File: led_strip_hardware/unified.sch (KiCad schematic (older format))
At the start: 36 parts, among them P1 mod_jack_in, P2 PWR_TST, P3 LED_STRIP, P4 ICSP, Q1 FDN5618P, SW1 USR_SW, U1 ISL83485IBZ, U2 TPS54560, U3 STM32F030-32, U4 NCP1117ST33T3G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

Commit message: Progress on v7 of led_strip_hardware
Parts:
- added C10: 2u2, SM1210, symbol C-RESCUE-unified
- added C11: 2u2, SA0805, symbol C-RESCUE-unified
- added C12: 100n, SA0402, symbol C-RESCUE-unified
- C1: footprint (none) -> SM1210; symbol C -> C-RESCUE-unified
- C2, C3, C4, C5, C8: footprint (none) -> SA0402; symbol C -> C-RESCUE-unified
- C6, C7: footprint (none) -> B6; symbol C -> C-RESCUE-unified
- C9: footprint (none) -> SA0805; symbol C -> C-RESCUE-unified
- D1: footprint (none) -> SA0603_LED; symbol LED -> LED-RESCUE-unified
- D2: footprint (none) -> DPAK3
- D3: footprint (none) -> DO-214AA(SMB)
- L1: footprint (none) -> MSS1210
- P1: footprint (none) -> Assman-6p4c
- P2, P3, P4: footprint (none) -> SIL-4
- Q1: footprint (none) -> SOT23GDS
- R1, R11, R12: footprint (none) -> SA0603; symbol R -> R-RESCUE-unified
- R10, R2, R3, R4, R7, R8, R9: footprint (none) -> SA0402; symbol R -> R-RESCUE-unified
- R5: value 68K -> 270K; footprint (none) -> SA0402; symbol R -> R-RESCUE-unified
- R6: value 12K -> 22K; footprint (none) -> SA0402; symbol R -> R-RESCUE-unified
- SW1: footprint (none) -> TACT-SW-SMD
- U1: footprint (none) -> SO8E
- U2: footprint MODULE -> SO8_WITH_EP
- U3: footprint MODULE -> LQFP32
- U4: footprint (none) -> SOT223
- U5: footprint (none) -> SOT23
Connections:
- net +48V: now also C10.1
- net 3V3: now also C11.1, C12.1
- net GND: now also C10.2, C11.2, C12.2
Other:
- note added: "12K"
- note added: "12V"
- note added: "5V"
- note added: "68K"
- note added: "Iin=700mA\nVin=48V"
- note added: "Iout=5A\nVout=5V"
- note added: "Pd=1.2W"
- note added: "Pd=100mW"
- note added: "Pd=2W"
- note added: "Pd=50mW"
- note added: "Pd=750mW"
- note added: "R5"
- note added: "R6"
- note added: "Total Pd=4.2W"
- note added: "Vpp"

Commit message: Progress on v7 of led_strip_hardware; some lux utilities
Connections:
- net at U3.27 (PB4): now also SW1.3
- net at U3.30 (PB7): no longer SW1.3
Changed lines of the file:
@@
 	5550 1950 5550 2500
 Wire Wire Line
-	5400 2500 5550 2500
-Wire Wire Line
-	5550 2500 5700 2500
+	5400 2500 5700 2500
 Wire Wire Line
 	5700 2500 5700 2800
@@
 	5700 3400 5700 3200
 Wire Wire Line
-	5400 3400 5550 3400
-Wire Wire Line
-	5550 3400 5700 3400
+	5400 3400 5700 3400
 Wire Wire Line
 	5550 3400 5550 3500
@@
 Connection ~ 6600 2250
 Wire Wire Line
-	6600 1750 6950 1750
-Wire Wire Line
-	6950 1750 7200 1750
-Wire Wire Line
-	7200 1750 7400 1750
-Wire Wire Line
-	7400 1750 7800 1750
+	6600 1750 7800 1750
 Connection ~ 6600 1750
 Connection ~ 6950 1750
@@
 $EndComp
 Wire Wire Line
-	8200 2300 8300 2300
-Wire Wire Line
-	8300 2300 8550 2300
-Wire Wire Line
-	8550 2300 8800 2300
+	8200 2300 8800 2300
 $Comp
 L GND-RESCUE-unified #PWR014
@@
 $EndComp
 Wire Wire Line
-	6500 3900 6700 3900
-Wire Wire Line
-	6700 3900 7450 3900
-Wire Wire Line
-	6300 3800 6900 3800
-Wire Wire Line
-	6900 3800 7450 3800
+	6500 3900 7450 3900
+Wire Wire Line
+	6300 3800 7450 3800
 $Comp
 L GND-RESCUE-unified #PWR023
@@
 	4900 4100 4800 4100
 Wire Wire Line
-	4800 4050 4800 4100
-Wire Wire Line
-	4800 4100 4800 4150
+	4800 4050 4800 4150
 Connection ~ 4800 4100
 Wire Wire Line
@@
 2x 16SVPF82M
 Wire Wire Line
-	6100 4100 6100 3900
-Wire Wire Line
-	6100 3900 5300 3900
+	5300 3900 6400 3900
 Wire Wire Line
 	5300 3900 5300 4600
@@
 Connection ~ 2300 2350
 Wire Wire Line
-	1150 1850 1850 1850
-Wire Wire Line
-	1850 1850 2300 1850
-Wire Wire Line
-	2300 1850 2500 1850
+	1150 1850 2500 1850
 $Comp
 L +48V #PWR040
@@
 	2300 2350 2700 2350
 Wire Wire Line
-	2900 1850 3150 1850
-Wire Wire Line
-	3150 1850 3350 1850
-Wire Wire Line
-	3350 1850 3650 1850
+	2900 1850 3650 1850
 $Comp
 L DIODESCH D3
@@
 	2750 3700 2750 3850
 Wire Wire Line
-	2750 3850 3000 3850
-Wire Wire Line
-	3000 3850 3200 3850
-Wire Wire Line
-	2750 4350 3000 4350
-Wire Wire Line
-	3000 4350 3200 4350
+	2750 3850 3200 3850
+Wire Wire Line
+	2750 4350 3200 4350
 Wire Wire Line
 	2750 4350 2750 4550
@@
 R5
 Text Notes 6200 1150 0    60   ~ 0
+12V
+Text Notes 6200 1250 0    60   ~ 0
 5V
-Text Notes 6200 1250 0    60   ~ 0
-12V
 Text Notes 7050 1250 0    60   ~ 0
 68K
@@
 Text Notes 7450 1900 0    60   ~ 0
 Total Pd=4.2W
+Wire Wire Line
+	6400 3900 6400 4100
 $EndSCHEMATC

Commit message: LED strip hardware rev 7; ready for prod?
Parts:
- SW1: value USR_SW -> TL3315NF160Q
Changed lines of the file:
@@
 	3400 4050 3200 4050
 Wire Wire Line
-	3200 3850 3200 4050
+	3200 4050 3200 3850
 Wire Wire Line
 	1500 1950 1500 4000
@@
 P 2950 5600
 F 0 "SW1" H 2950 5900 60  0000 C CNN
-F 1 "USR_SW" H 2950 5450 60  0000 C CNN
+F 1 "TL3315NF160Q" H 2950 5450 60  0000 C CNN
 F 2 "TACT-SW-SMD" H 2950 5350 30  0000 C CNN
 F 3 "" H 2950 5600 60  0000 C CNN

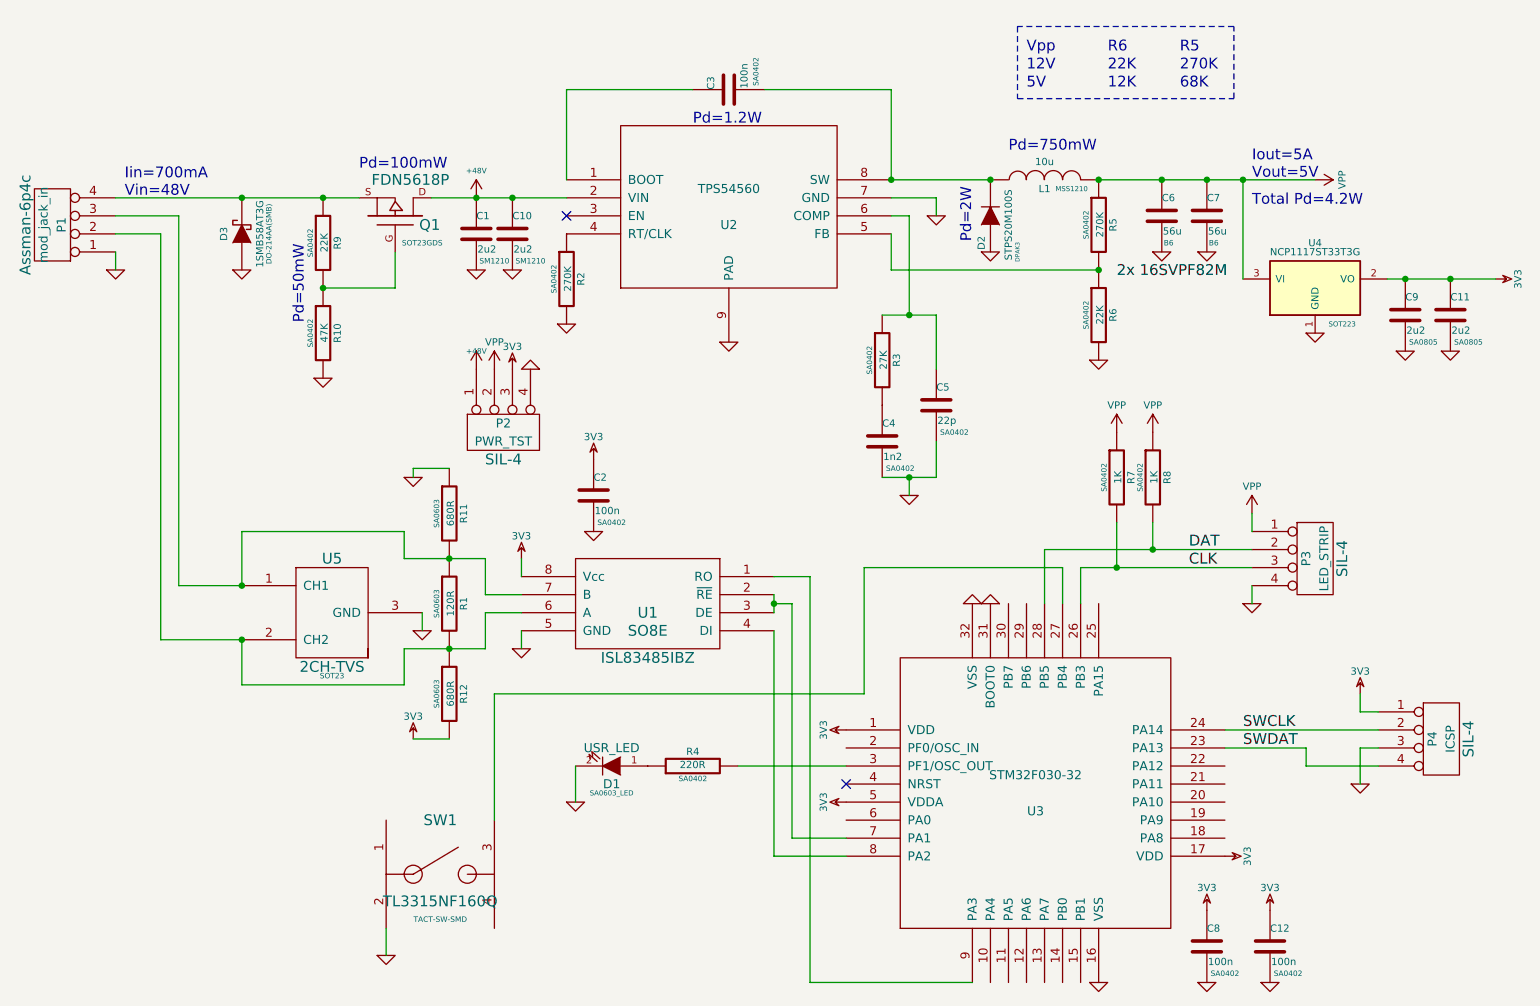
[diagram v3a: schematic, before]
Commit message: Flipped D2; still need to fix silk bottom
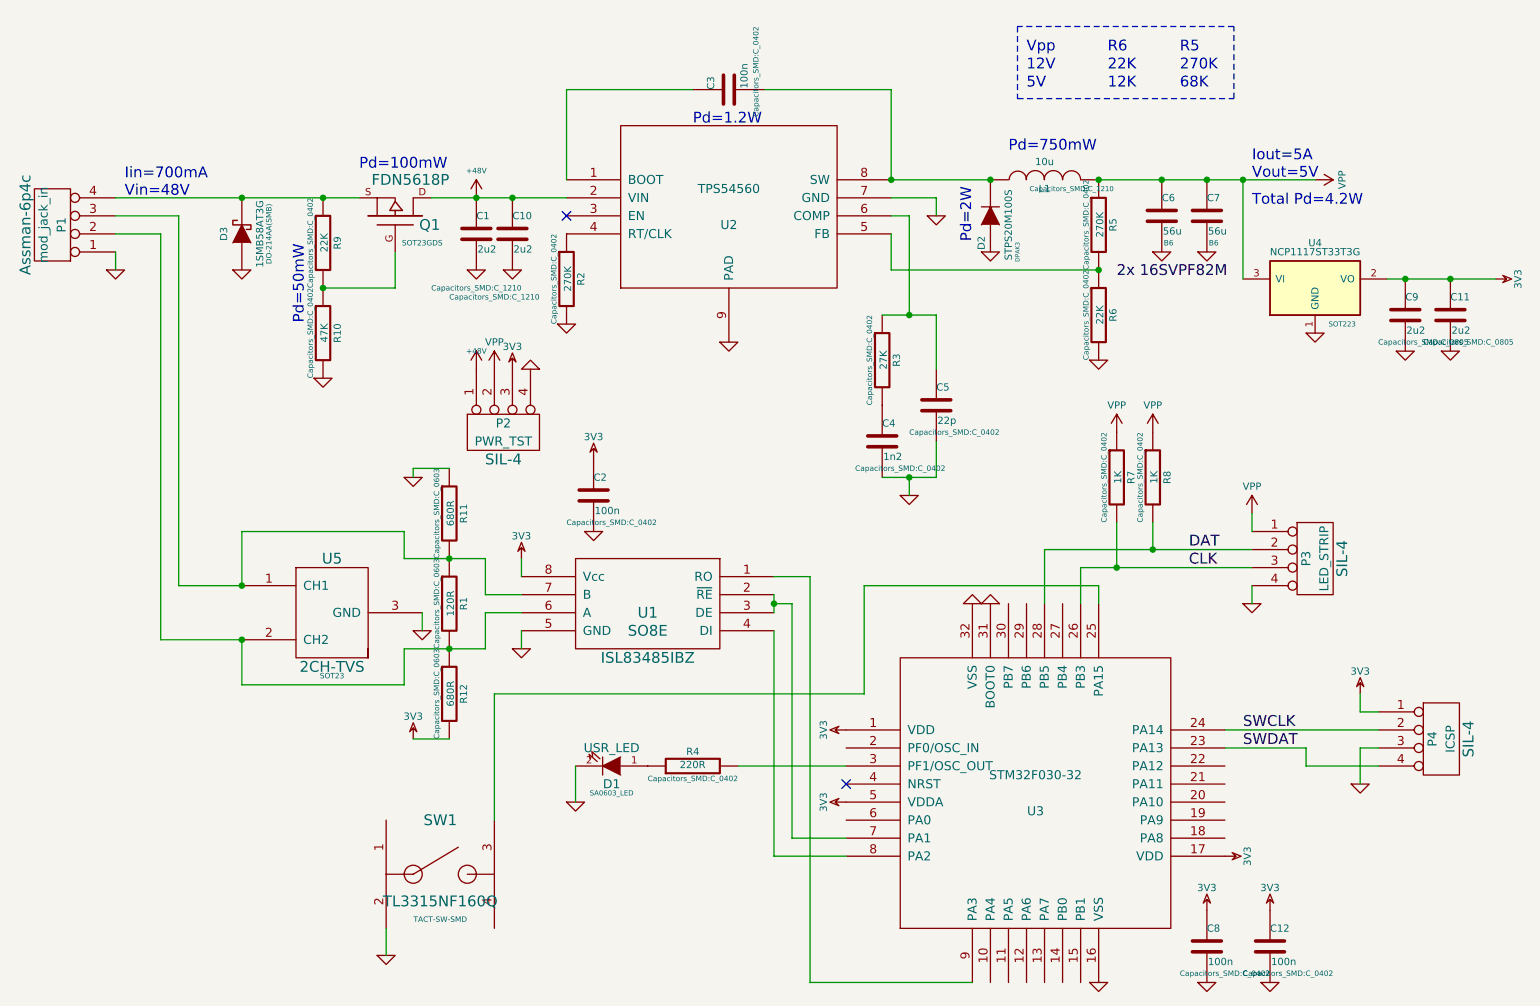
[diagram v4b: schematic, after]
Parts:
- C1, C10: footprint SM1210 -> Capacitors_SMD:C_1210
- C11, C9: footprint SA0805 -> Capacitors_SMD:C_0805
- C12, C2, C3, C4, C5, C8, R10, R2, R3, R4, R5, R6, R7, R8, R9: footprint SA0402 -> Capacitors_SMD:C_0402
- L1: footprint MSS1210 -> Capacitors_SMD:C_1210
- R1, R11, R12: footprint SA0603 -> Capacitors_SMD:C_0603
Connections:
- net at U3.25 (PA15): now also SW1.3
- net at U3.27 (PB4): no longer SW1.3
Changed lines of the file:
@@
 F 0 "C1" H 3150 2150 40  0000 L CNN
 F 1 "2u2" H 3156 1965 40  0000 L CNN
-F 2 "SM1210" H 3250 1900 30  0000 C CNN
+F 2 "Capacitors_SMD:C_1210" H 3150 1750 30  0000 C CNN
 F 3 "" H 3150 2050 60  0000 C CNN
 	1    3150 2050
@@
 F 0 "R2" V 3730 2300 40  0000 C CNN
 F 1 "270K" V 3657 2301 40  0000 C CNN
-F 2 "SA0402" V 3580 2300 30  0000 C CNN
+F 2 "Capacitors_SMD:C_0402" V 3580 2300 30  0000 C CNN
 F 3 "" H 3650 2300 30  0000 C CNN
 	1    3650 2300
@@
 F 0 "C3" H 4550 1350 40  0000 L CNN
 F 1 "100n" H 4556 1165 40  0000 L CNN
-F 2 "SA0402" H 4650 1100 30  0000 C CNN
+F 2 "Capacitors_SMD:C_0402" H 4650 1100 30  0000 C CNN
 F 3 "" H 4550 1250 60  0000 C CNN
 	1    4550 1250
@@
 F 0 "L1" V 6250 1750 40  0000 C CNN
 F 1 "10u" V 6400 1750 40  0000 C CNN
-F 2 "MSS1210" V 6250 1600 28  0000 C CNN
+F 2 "Capacitors_SMD:C_1210" V 6250 1600 28  0000 C CNN
 F 3 "" H 6300 1750 60  0000 C CNN
 	1    6300 1750
@@
 F 0 "R5" V 6680 2000 40  0000 C CNN
 F 1 "270K" V 6607 2001 40  0000 C CNN
-F 2 "SA0402" V 6530 2000 30  0000 C CNN
+F 2 "Capacitors_SMD:C_0402" V 6530 2000 30  0000 C CNN
 F 3 "" H 6600 2000 30  0000 C CNN
 	1    6600 2000
@@
 F 0 "R6" V 6680 2500 40  0000 C CNN
 F 1 "22K" V 6607 2501 40  0000 C CNN
-F 2 "SA0402" V 6530 2500 30  0000 C CNN
+F 2 "Capacitors_SMD:C_0402" V 6530 2500 30  0000 C CNN
 F 3 "" H 6600 2500 30  0000 C CNN
 	1    6600 2500
@@
 F 0 "R3" V 5480 2750 40  0000 C CNN
 F 1 "27K" V 5407 2751 40  0000 C CNN
-F 2 "SA0402" V 5330 2750 30  0000 C CNN
+F 2 "Capacitors_SMD:C_0402" V 5330 2750 30  0000 C CNN
 F 3 "" H 5400 2750 30  0000 C CNN
 	1    5400 2750
@@
 F 0 "C4" H 5400 3300 40  0000 L CNN
 F 1 "1n2" H 5406 3115 40  0000 L CNN
-F 2 "SA0402" H 5500 3050 30  0000 C CNN
+F 2 "Capacitors_SMD:C_0402" H 5500 3050 30  0000 C CNN
 F 3 "" H 5400 3200 60  0000 C CNN
 	1    5400 3200
@@
 F 0 "C5" H 5700 3100 40  0000 L CNN
 F 1 "22p" H 5706 2915 40  0000 L CNN
-F 2 "SA0402" H 5800 2850 30  0000 C CNN
+F 2 "Capacitors_SMD:C_0402" H 5800 2850 30  0000 C CNN
 F 3 "" H 5700 3000 60  0000 C CNN
 	1    5700 3000
@@
 F 0 "R1" V 3080 4100 40  0000 C CNN
 F 1 "120R" V 3007 4101 40  0000 C CNN
-F 2 "SA0603" V 2930 4100 30  0000 C CNN
+F 2 "Capacitors_SMD:C_0603" V 2930 4100 30  0000 C CNN
 F 3 "" H 3000 4100 30  0000 C CNN
 	1    3000 4100
@@
 	3400 4050 3200 4050
 Wire Wire Line
-	3200 4050 3200 3850
+	3200 3850 3200 4050
 Wire Wire Line
 	1500 1950 1500 4000
@@
 F 0 "C9" H 8300 2600 40  0000 L CNN
 F 1 "2u2" H 8306 2415 40  0000 L CNN
-F 2 "SA0805" H 8400 2350 30  0000 C CNN
+F 2 "Capacitors_SMD:C_0805" H 8400 2350 30  0000 C CNN
 F 3 "" H 8300 2500 60  0000 C CNN
 	1    8300 2500
@@
 F 0 "R7" V 6780 3400 40  0000 C CNN
 F 1 "1K" V 6707 3401 40  0000 C CNN
-F 2 "SA0402" V 6630 3400 30  0000 C CNN
+F 2 "Capacitors_SMD:C_0402" V 6630 3400 30  0000 C CNN
 F 3 "" H 6700 3400 30  0000 C CNN
 	1    6700 3400
@@
 F 0 "R8" V 6980 3400 40  0000 C CNN
 F 1 "1K" V 6907 3401 40  0000 C CNN
-F 2 "SA0402" V 6830 3400 30  0000 C CNN
+F 2 "Capacitors_SMD:C_0402" V 6830 3400 30  0000 C CNN
 F 3 "" H 6900 3400 30  0000 C CNN
 	1    6900 3400
@@
 F 0 "C2" H 3800 3600 40  0000 L CNN
 F 1 "100n" H 3806 3415 40  0000 L CNN
-F 2 "SA0402" H 3900 3350 30  0000 C CNN
+F 2 "Capacitors_SMD:C_0402" H 3900 3350 30  0000 C CNN
 F 3 "" H 3800 3500 60  0000 C CNN
 	1    3800 3500
@@
 F 0 "C8" H 7200 6100 40  0000 L CNN
 F 1 "100n" H 7206 5915 40  0000 L CNN
-F 2 "SA0402" H 7300 5850 30  0000 C CNN
+F 2 "Capacitors_SMD:C_0402" H 7300 5850 30  0000 C CNN
 F 3 "" H 7200 6000 60  0000 C CNN
 	1    7200 6000
@@
 F 0 "R4" V 4430 5000 40  0000 C CNN
 F 1 "220R" V 4357 5001 40  0000 C CNN
-F 2 "SA0402" V 4280 5000 30  0000 C CNN
+F 2 "Capacitors_SMD:C_0402" V 4280 5000 30  0000 C CNN
 F 3 "" H 4350 5000 30  0000 C CNN
 	1    4350 5000
@@
 2x 16SVPF82M
 Wire Wire Line
-	5300 3900 6400 3900
-Wire Wire Line
-	5300 3900 5300 4600
+	5300 4000 6600 4000
+Wire Wire Line
+	5300 4000 5300 4600
 Wire Wire Line
 	5300 4600 3250 4600
@@
 F 0 "R9" V 2380 2100 40  0000 C CNN
 F 1 "22K" V 2307 2101 40  0000 C CNN
-F 2 "SA0402" V 2230 2100 30  0000 C CNN
+F 2 "Capacitors_SMD:C_0402" V 2230 2100 30  0000 C CNN
 F 3 "" H 2300 2100 30  0000 C CNN
 	1    2300 2100
@@
 F 0 "R10" V 2380 2600 40  0000 C CNN
 F 1 "47K" V 2307 2601 40  0000 C CNN
-F 2 "SA0402" V 2230 2600 30  0000 C CNN
+F 2 "Capacitors_SMD:C_0402" V 2230 2600 30  0000 C CNN
 F 3 "" H 2300 2600 30  0000 C CNN
 	1    2300 2600
@@
 F 0 "R11" V 3080 3600 40  0000 C CNN
 F 1 "680R" V 3007 3601 40  0000 C CNN
-F 2 "SA0603" V 2930 3600 30  0000 C CNN
+F 2 "Capacitors_SMD:C_0603" V 2930 3600 30  0000 C CNN
 F 3 "" H 3000 3600 30  0000 C CNN
 	1    3000 3600
@@
 F 0 "R12" V 3080 4600 40  0000 C CNN
 F 1 "680R" V 3007 4601 40  0000 C CNN
-F 2 "SA0603" V 2930 4600 30  0000 C CNN
+F 2 "Capacitors_SMD:C_0603" V 2930 4600 30  0000 C CNN
 F 3 "" H 3000 4600 30  0000 C CNN
 	1    3000 4600
@@
 F 0 "C12" H 7550 6100 40  0000 L CNN
 F 1 "100n" H 7556 5915 40  0000 L CNN
-F 2 "SA0402" H 7650 5850 30  0000 C CNN
+F 2 "Capacitors_SMD:C_0402" H 7650 5850 30  0000 C CNN
 F 3 "" H 7550 6000 60  0000 C CNN
 	1    7550 6000
@@
 F 0 "C10" H 3350 2150 40  0000 L CNN
 F 1 "2u2" H 3356 1965 40  0000 L CNN
-F 2 "SM1210" H 3450 1900 30  0000 C CNN
+F 2 "Capacitors_SMD:C_1210" H 3250 1700 30  0000 C CNN
 F 3 "" H 3350 2050 60  0000 C CNN
 	1    3350 2050
@@
 F 0 "C11" H 8550 2600 40  0000 L CNN
 F 1 "2u2" H 8556 2415 40  0000 L CNN
-F 2 "SA0805" H 8650 2350 30  0000 C CNN
+F 2 "Capacitors_SMD:C_0805" H 8650 2350 30  0000 C CNN
 F 3 "" H 8550 2500 60  0000 C CNN
 	1    8550 2500
@@
 Total Pd=4.2W
 Wire Wire Line
-	6400 3900 6400 4100
+	6600 4000 6600 4100
 $EndSCHEMATC

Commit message: LED Strip rev 8
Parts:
- removed C11: 2u2, Capacitors_SMD:C_0805, symbol C-RESCUE-unified
- C1, C10: value 2u2 -> 4u7; Part (none) -> C3225X7S2A475M200AB
- C6, C7: value 56u -> 82u; Part (none) -> 16SVPF82M
- L1: value 10u -> XAL6060-103MEB
- Q1: value FDN5618P -> CPH3351-TL-W
- R5: value 270K -> 68K
- R6: value 22K -> 12K
- U5: value 2CH-TVS -> TPD2E2U06QDBZRQ1
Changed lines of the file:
@@
 P 3150 2050
 F 0 "C1" H 3150 2150 40  0000 L CNN
-F 1 "2u2" H 3156 1965 40  0000 L CNN
+F 1 "4u7" H 3156 1965 40  0000 L CNN
 F 2 "Capacitors_SMD:C_1210" H 3150 1750 30  0000 C CNN
 F 3 "" H 3150 2050 60  0000 C CNN
+F 4 "C3225X7S2A475M200AB" H 3150 2050 60  0001 C CNN "Part"
 	1    3150 2050
 	1    0    0    -1
@@
 P 6300 1750
 F 0 "L1" V 6250 1750 40  0000 C CNN
-F 1 "10u" V 6400 1750 40  0000 C CNN
+F 1 "XAL6060-103MEB" V 6400 1750 40  0000 C CNN
 F 2 "Capacitors_SMD:C_1210" V 6250 1600 28  0000 C CNN
 F 3 "" H 6300 1750 60  0000 C CNN
@@
 P 6600 2000
 F 0 "R5" V 6680 2000 40  0000 C CNN
-F 1 "270K" V 6607 2001 40  0000 C CNN
+F 1 "68K" V 6607 2001 40  0000 C CNN
 F 2 "Capacitors_SMD:C_0402" V 6530 2000 30  0000 C CNN
 F 3 "" H 6600 2000 30  0000 C CNN
@@
 P 6600 2500
 F 0 "R6" V 6680 2500 40  0000 C CNN
-F 1 "22K" V 6607 2501 40  0000 C CNN
+F 1 "12K" V 6607 2501 40  0000 C CNN
 F 2 "Capacitors_SMD:C_0402" V 6530 2500 30  0000 C CNN
 F 3 "" H 6600 2500 30  0000 C CNN
@@
 P 6950 1950
 F 0 "C6" H 6950 2050 40  0000 L CNN
-F 1 "56u" H 6956 1865 40  0000 L CNN
+F 1 "82u" H 6956 1865 40  0000 L CNN
 F 2 "B6" H 6988 1800 30  0000 C CNN
 F 3 "" H 6950 1950 60  0000 C CNN
+F 4 "16SVPF82M" H 6950 1950 60  0001 C CNN "Part"
 	1    6950 1950
 	1    0    0    -1
@@
 P 7200 1950
 F 0 "C7" H 7200 2050 40  0000 L CNN
-F 1 "56u" H 7206 1865 40  0000 L CNN
+F 1 "82u" H 7206 1865 40  0000 L CNN
 F 2 "B6" H 7238 1800 30  0000 C CNN
 F 3 "" H 7200 1950 60  0000 C CNN
+F 4 "16SVPF82M" H 7200 1950 60  0001 C CNN "Part"
 	1    7200 1950
 	1    0    0    -1
@@
 	5550 1950 5550 2500
 Wire Wire Line
-	5400 2500 5700 2500
+	5400 2500 5550 2500
+Wire Wire Line
+	5550 2500 5700 2500
 Wire Wire Line
 	5700 2500 5700 2800
@@
 	5700 3400 5700 3200
 Wire Wire Line
-	5400 3400 5700 3400
+	5400 3400 5550 3400
+Wire Wire Line
+	5550 3400 5700 3400
 Wire Wire Line
 	5550 3400 5550 3500
@@
 Connection ~ 6600 2250
 Wire Wire Line
-	6600 1750 7800 1750
+	6600 1750 6950 1750
+Wire Wire Line
+	6950 1750 7200 1750
+Wire Wire Line
+	7200 1750 7400 1750
+Wire Wire Line
+	7400 1750 7800 1750
 Connection ~ 6600 1750
 Connection ~ 6950 1750
@@
 $EndComp
 Wire Wire Line
-	8200 2300 8800 2300
+	8200 2300 8300 2300
+Wire Wire Line
+	8300 2300 8550 2300
 $Comp
 L GND-RESCUE-unified #PWR014
@@
 L 3V3 #PWR015
 U 1 1 54CC22D0
-P 8800 2300
-F 0 "#PWR015" H 8800 2400 40  0001 C CNN
-F 1 "3V3" H 8800 2425 40  0000 C CNN
-F 2 "" H 8800 2300 60  0000 C CNN
-F 3 "" H 8800 2300 60  0000 C CNN
-	1    8800 2300
+P 8550 2300
+F 0 "#PWR015" H 8550 2400 40  0001 C CNN
+F 1 "3V3" H 8550 2425 40  0000 C CNN
+F 2 "" H 8550 2300 60  0000 C CNN
+F 3 "" H 8550 2300 60  0000 C CNN
+	1    8550 2300
 	0    1    1    0
 $EndComp
@@
 $EndComp
 Wire Wire Line
-	6500 3900 7450 3900
-Wire Wire Line
-	6300 3800 7450 3800
+	6500 3900 6700 3900
+Wire Wire Line
+	6700 3900 7450 3900
+Wire Wire Line
+	6300 3800 6900 3800
+Wire Wire Line
+	6900 3800 7450 3800
 $Comp
 L GND-RESCUE-unified #PWR023
@@
 	4900 4100 4800 4100
 Wire Wire Line
-	4800 4050 4800 4150
+	4800 4050 4800 4100
+Wire Wire Line
+	4800 4100 4800 4150
 Connection ~ 4800 4100
 Wire Wire Line
@@
 P 2700 1950
 F 0 "Q1" V 2650 2200 60  0000 R CNN
-F 1 "FDN5618P" V 2900 2250 60  0000 R CNN
+F 1 "CPH3351-TL-W" V 2900 2250 60  0000 R CNN
 F 2 "SOT23GDS" V 2550 2100 30  0000 C CNN
 F 3 "" H 2700 1950 60  0000 C CNN
@@
 Connection ~ 2300 2350
 Wire Wire Line
-	1150 1850 2500 1850
+	1150 1850 1850 1850
+Wire Wire Line
+	1850 1850 2300 1850
+Wire Wire Line
+	2300 1850 2500 1850
 $Comp
 L +48V #PWR040
@@
 	2300 2350 2700 2350
 Wire Wire Line
-	2900 1850 3650 1850
+	2900 1850 3150 1850
+Wire Wire Line
+	3150 1850 3350 1850
+Wire Wire Line
+	3350 1850 3650 1850
 $Comp
 L DIODESCH D3
@@
 P 2350 4150
 F 0 "U5" H 2350 4450 60  0000 C CNN
-F 1 "2CH-TVS" H 2350 3850 60  0000 C CNN
+F 1 "TPD2E2U06QDBZRQ1" H 2350 3850 60  0000 C CNN
 F 2 "SOT23" H 2350 3800 30  0000 C CNN
 F 3 "" H 2350 4150 60  0000 C CNN
@@
 	2750 3700 2750 3850
 Wire Wire Line
-	2750 3850 3200 3850
-Wire Wire Line
-	2750 4350 3200 4350
+	2750 3850 3000 3850
+Wire Wire Line
+	3000 3850 3200 3850
+Wire Wire Line
+	2750 4350 3000 4350
+Wire Wire Line
+	3000 4350 3200 4350
 Wire Wire Line
 	2750 4350 2750 4550
@@
 P 3350 2050
 F 0 "C10" H 3350 2150 40  0000 L CNN
-F 1 "2u2" H 3356 1965 40  0000 L CNN
+F 1 "4u7" H 3356 1965 40  0000 L CNN
 F 2 "Capacitors_SMD:C_1210" H 3250 1700 30  0000 C CNN
 F 3 "" H 3350 2050 60  0000 C CNN
+F 4 "C3225X7S2A475M200AB" H 3350 2050 60  0001 C CNN "Part"
 	1    3350 2050
 	1    0    0    -1
@@
 	1    0    0    -1
 $EndComp
-$Comp
-L C-RESCUE-unified C11
-U 1 1 57257921
-P 8550 2500
-F 0 "C11" H 8550 2600 40  0000 L CNN
-F 1 "2u2" H 8556 2415 40  0000 L CNN
-F 2 "Capacitors_SMD:C_0805" H 8650 2350 30  0000 C CNN
-F 3 "" H 8550 2500 60  0000 C CNN
-	1    8550 2500
-	1    0    0    -1
-$EndComp
-$Comp
-L GND-RESCUE-unified #PWR048
-U 1 1 572579BE
-P 8550 2700
-F 0 "#PWR048" H 8550 2700 30  0001 C CNN
-F 1 "GND" H 8550 2630 30  0001 C CNN
-F 2 "" H 8550 2700 60  0000 C CNN
-F 3 "" H 8550 2700 60  0000 C CNN
-	1    8550 2700
-	1    0    0    -1
-$EndComp
 Connection ~ 3350 1850
-Connection ~ 8550 2300
 Text Notes 2500 1700 0    60   ~ 0
 Pd=100mW
